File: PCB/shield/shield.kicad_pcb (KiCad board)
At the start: 2 copper layers, 99.6 x 80.1 mm, 18 parts, among them J1 QTR-8A, J10 ESP32_left_m, J11 ESP32_right_m, J12 Barrel_Jack, J13 Conn_01x06, J14 Domino, J15 Domino, J2 QMC5883L, J3 Servo, J8 ESP32_left_f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

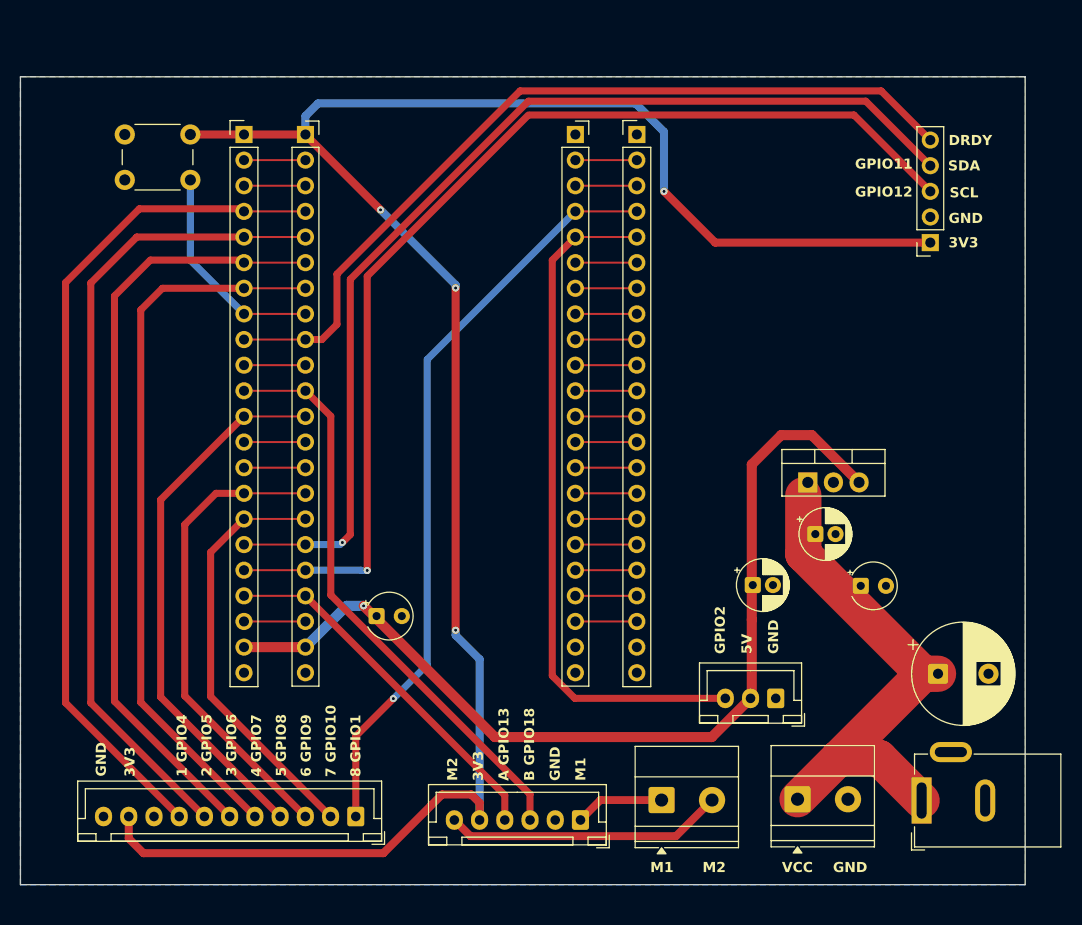
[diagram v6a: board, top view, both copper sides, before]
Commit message: fix: increased distance between esp rails
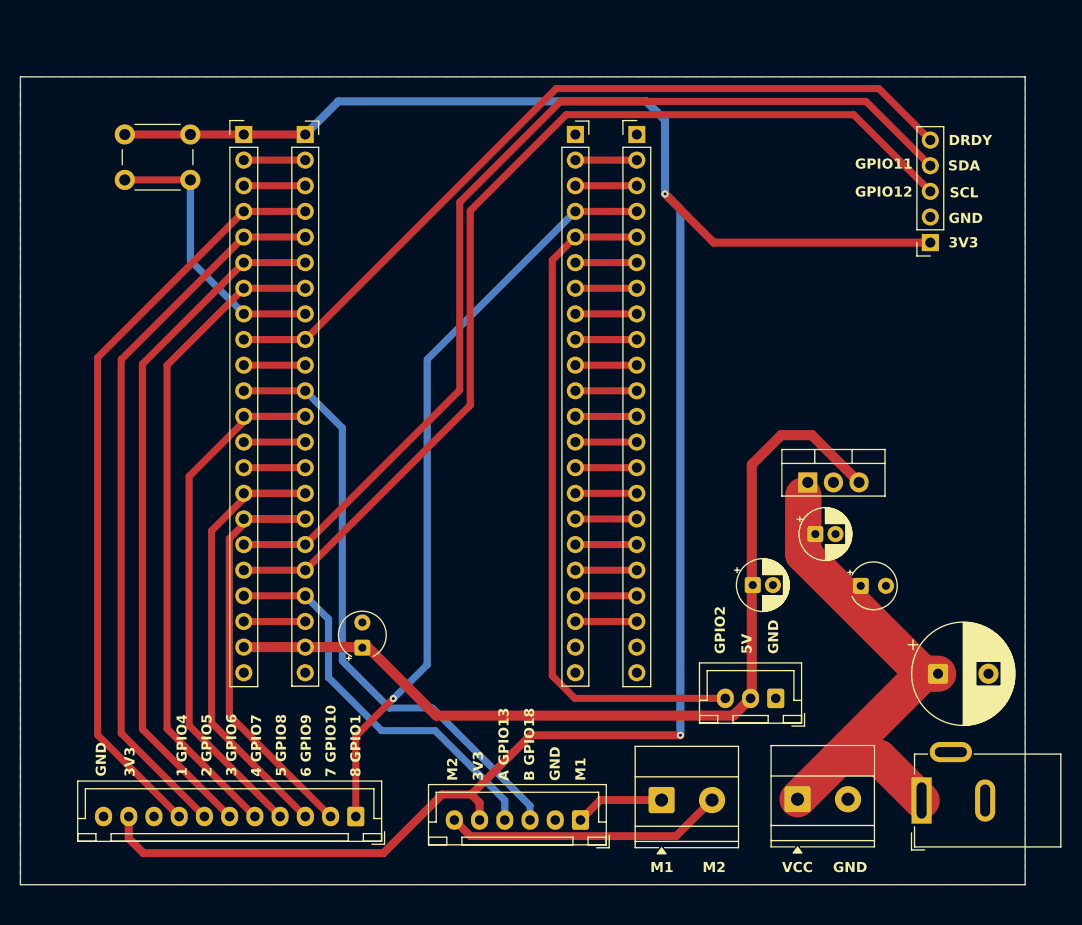
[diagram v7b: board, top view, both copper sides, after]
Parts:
- moved C5 3.44 mm to (121.5, 123.6), turned to 90 degrees
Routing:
- net /GPIO15: track 21.6 -> 34.2 mm
- net /GPIO10: track 41.9 -> 52.2 mm
- net /GPIO8: track 54.1 -> 63.6 mm
- net +3V3: track 201.9 -> 210.7 mm, vias 4 -> 2
- net /GPIO9: track 47.1 -> 55.2 mm
- net Net-(J10-Pin_3): track 6.09 -> 12.2 mm
- net Net-(J10-Pin_2): track 6.09 -> 12.2 mm
- net Net-(J10-Pin_14): track 6.09 -> 12.2 mm
- net Net-(J10-Pin_13): track 6.09 -> 12.2 mm
- net /GPIO17: track 6.09 -> 12.2 mm
- net /GPIO14: track 6.09 -> 12.2 mm
- net +5V: track 95.9 -> 90.6 mm, vias 1 -> 0
- net /GPIO13: track 36.5 -> 39.6 mm
- net /GPIO4: track 84.5 -> 81.5 mm
- net /GPIO16: track 83.2 -> 80.4 mm
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
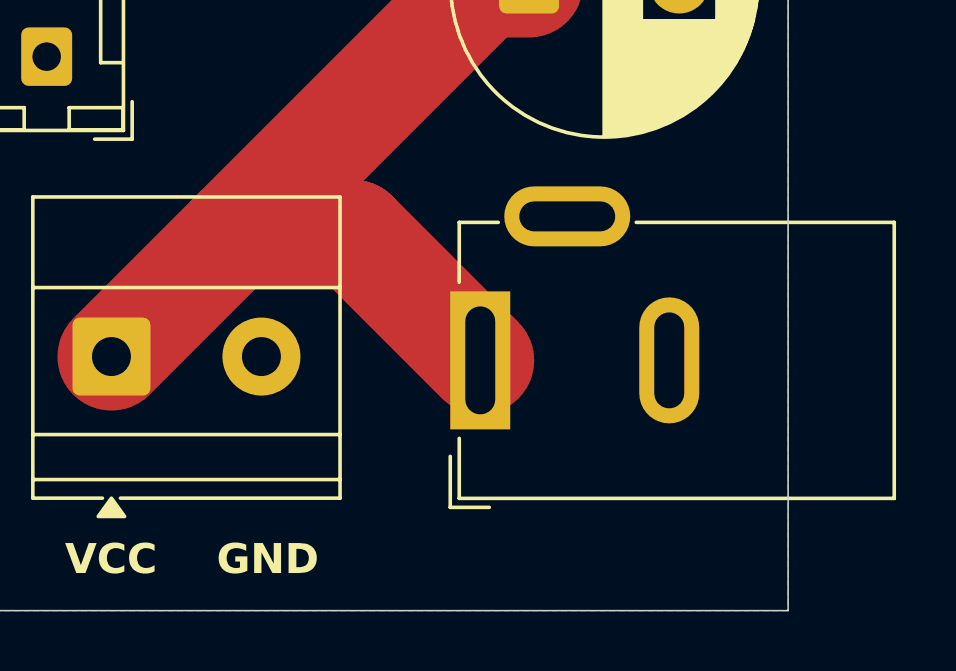
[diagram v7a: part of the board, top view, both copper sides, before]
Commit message: feat: changed 5.5 jack to domino terminal
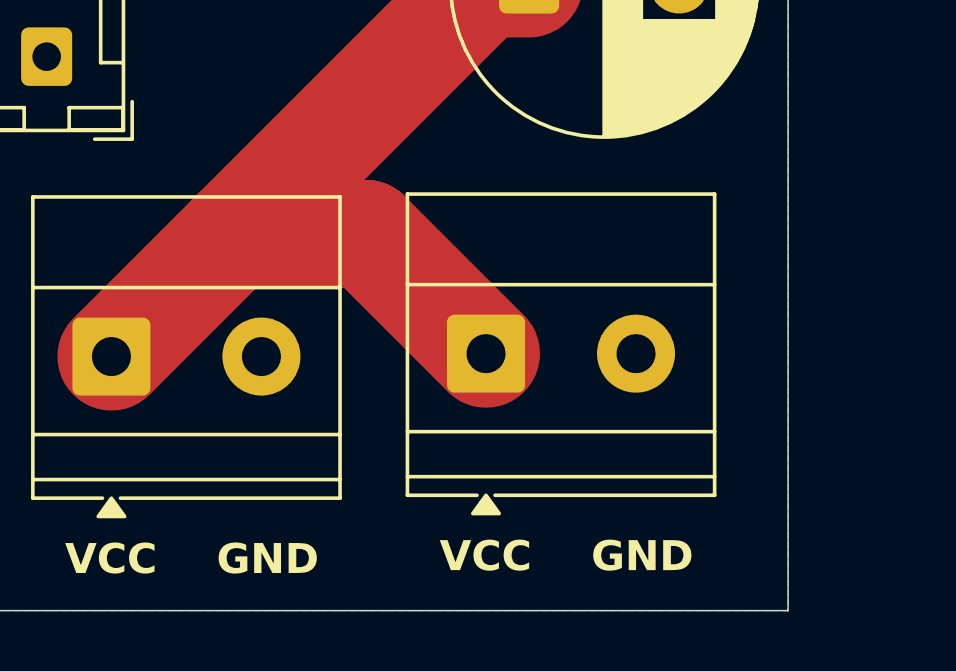
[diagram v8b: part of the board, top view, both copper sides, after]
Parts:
- removed J12: Barrel_Jack, Connector_BarrelJack:BarrelJack_GCT_DCJ200-10-A_Horizontal
- added J15: Domino, TerminalBlock_Phoenix:TerminalBlock_Phoenix_MKDS-1,5-2_1x02_P5.00mm_Horizontal, F.Cu at (177.1, 138.5)
